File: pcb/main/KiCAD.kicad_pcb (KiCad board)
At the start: 2 copper layers, 366.4 x 137.2 mm, 366 parts, among them Q1 2N7002, SW10 CherryMX, SW11 CherryMX, SW12 CherryMX, SW13 CherryMX, SW14 CherryMX, SW15 CherryMX, SW16 CherryMX, SW17 CherryMX, SW18 CherryMX, SW19 CherryMX, SW2 CherryMX, SW20 CherryMX, SW21 CherryMX, SW22 CherryMX, SW23 CherryMX, SW24 CherryMX, SW25 CherryMX, SW26 CherryMX, SW27 CherryMX, SW28 CherryMX, SW29 CherryMX, SW3 CherryMX, SW30 CherryMX, SW31 CherryMX, SW32 CherryMX, SW33 CherryMX, SW34 CherryMX, SW35 CherryMX, SW36 CherryMX, SW37 CherryMX, SW38 CherryMX, SW39 CherryMX, SW4 CherryMX, SW40 CherryMX, SW41 CherryMX, SW42 CherryMX, SW43 CherryMX, SW44 CherryMX, SW45 CherryMX, SW46 CherryMX, SW47 CherryMX, SW48 CherryMX, SW49 CherryMX, SW5 CherryMX, SW50 CherryMX, SW51 CherryMX, SW52 CherryMX, SW53 CherryMX, SW54 CherryMX, SW55 CherryMX, SW56 CherryMX, SW57 CherryMX, SW58 CherryMX, SW59 CherryMX, SW6 CherryMX, SW60 CherryMX, SW61 CherryMX, SW62 CherryMX, SW63 CherryMX, SW64 CherryMX, SW65 CherryMX, SW66 CherryMX, SW67 CherryMX, SW68 CherryMX, SW69 CherryMX, SW7 CherryMX, SW70 CherryMX, SW71 CherryMX, SW72 CherryMX, SW73 CherryMX, SW74 CherryMX, SW75 CherryMX, SW76 CherryMX, SW77 CherryMX, SW78 CherryMX, SW79 CherryMX, SW8 CherryMX, SW80 CherryMX, SW81 CherryMX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

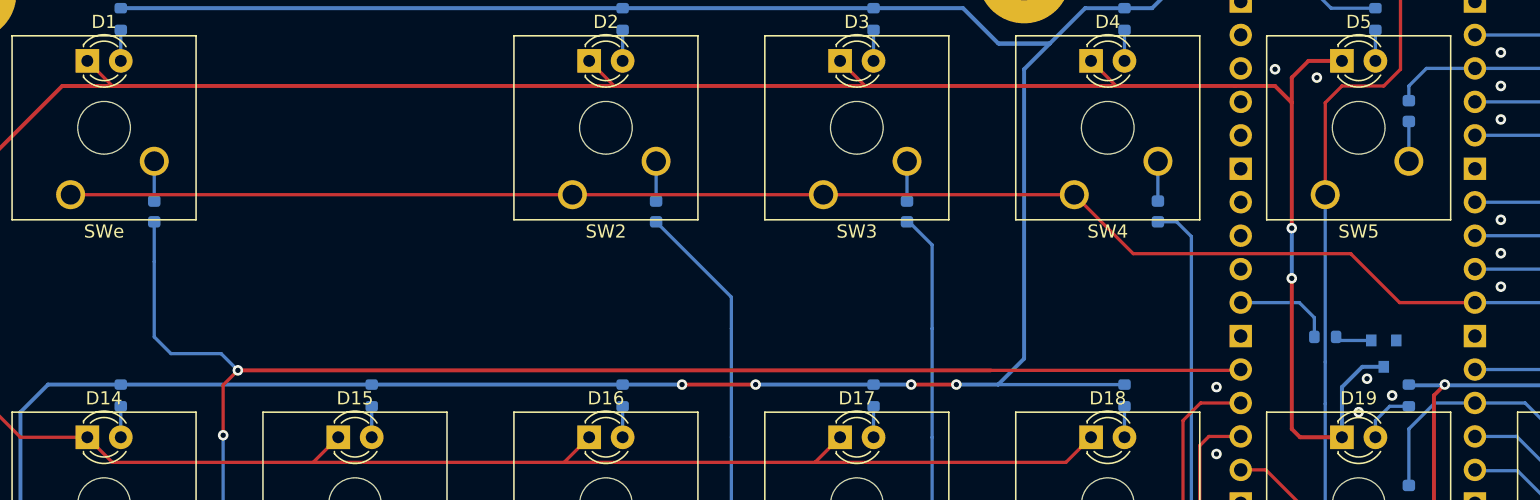
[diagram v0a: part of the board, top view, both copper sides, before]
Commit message: step ファイルの追加
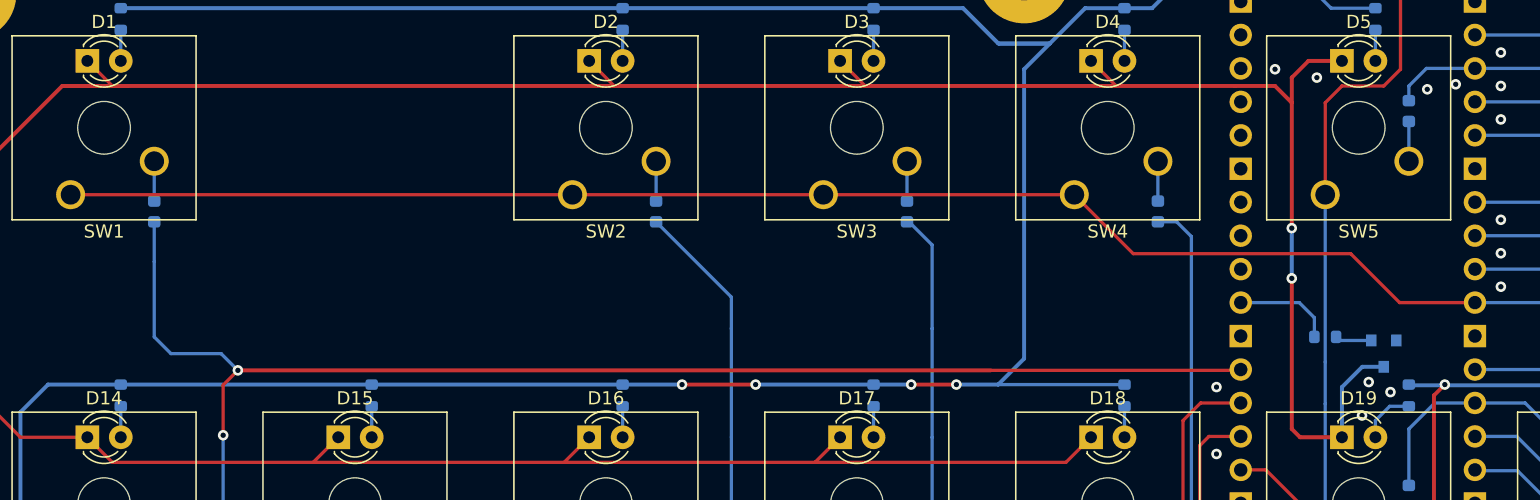
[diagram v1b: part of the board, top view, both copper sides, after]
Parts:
- R88: value 1k -> 100
- renumbered SWe to SW1
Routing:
- net GND: vias 195 -> 197

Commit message: とりあえず自分なりにベタグランドのアンテナを除去した
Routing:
- net Net-(D1-Pad1): vias 19 -> 20
- net GND: vias 197 -> 249
- net (no net): vias 2 -> 0

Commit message: ベタグランドのアンテナを除去してデザインルールチェックも済ませた.
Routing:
- net Net-(D1-Pad1): vias 20 -> 19
- net GND: vias 249 -> 300

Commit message: 2u キーにスタビライザを適応
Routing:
- net VBUS: track 2957.7 -> 2853.5 mm
- net Row4: track 275.0 -> 285.1 mm
- net Col6: track 331.6 -> 339.2 mm, vias 4 -> 6
- net Col2: track 646.6 -> 652.5 mm
- net Net-(D1-Pad1): track 2950.2 -> 2951.6 mm
- net Col1: track 313.9 -> 314.8 mm
